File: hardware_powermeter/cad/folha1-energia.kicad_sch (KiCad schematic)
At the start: 24 parts, among them J101 conector magnetico 6 vias, J102 JST SM02B-SRSS-TB, U101 nPM1100-QDAB, U102 MAX17048G+T10

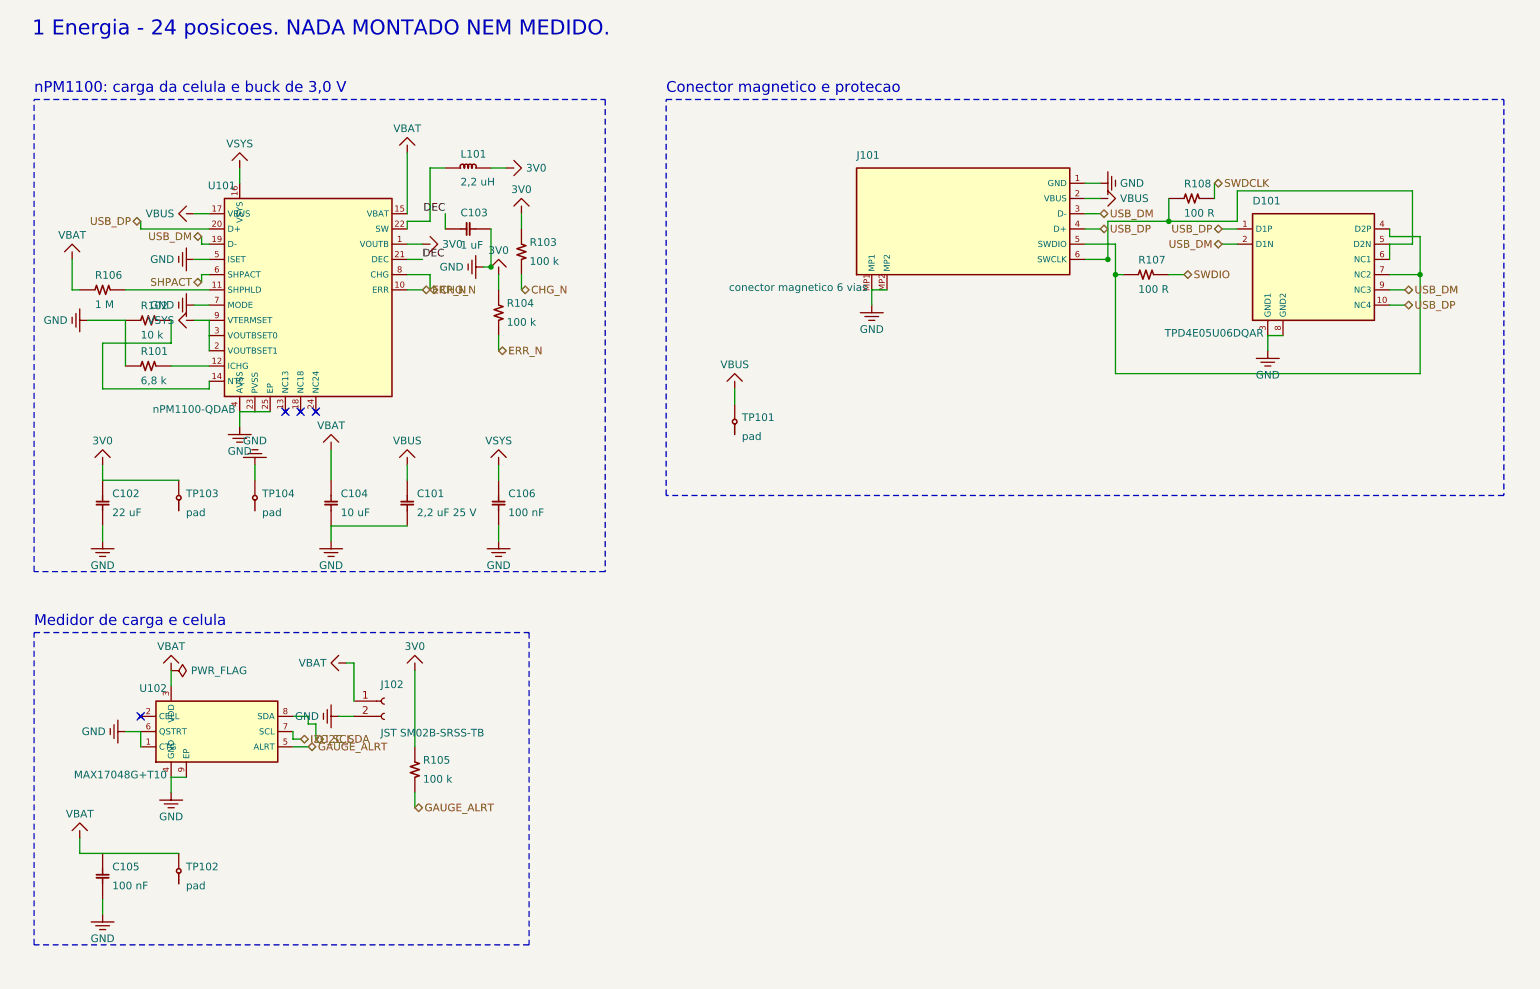
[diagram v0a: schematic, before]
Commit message: feat(hardware): 48 x 16 mm board and a 53,4 x 19,4 x 8,5 mm pod
The board came down from 60 to 48 mm and the pod from 65,4 x 19,4 x 10,5
to 53,4 x 19,4 x 8,5, with the mass estimate at 11,4 g against the 20 g
of the class. The height now meets the target exactly, because the cell
shrank from 4,0 to 2,5 mm: the owner's 5 kOhm decision takes the meter
from 3,9 to 1,5 mA while pedalling, so 50 hours ask for about 75 mAh and
a 100 mAh pouch is enough. The six-way connector stays, in two rows of
three instead of a single row, which gave back about 7 mm of length
without losing a way, and the Tag-Connect went: with SWD on the cable it
was duplicated copper.

It is NOT manufacturable yet, and the numbers say why rather than a
hopeful adjective: the design rule check finds 0 errors but 16
connections still open. One of them, ERR_N, has no copper at all while
the router reported "98 routed, 0 nets left out", so the router's own
accounting is wrong, not just its routing. Disabling the pruning of
dangling tracks was tried first and changed nothing, which clears the
pruning. A second routing pass made it worse, 21 open and three pairs of
vias too close: the pass is not incremental, it re-routes from scratch
into a different result.

Two more real defects are recorded: the placer cannot seat C403 and
C308, carrying them 11 to 13 mm from the part they decouple, and three
pod rules fail, the back-face bodies against the cell, the rib at zero
and a back pad under a pillar.

The layer drawings print properly for the first time. kicad-cli 8.0.6
does not have --page-size-mode or --exclude-drawing-sheet, which are
KiCad 9 options, so the export was failing outright and, before that,
putting a 1:1 board in the corner of an empty sheet. The flags are now
tried and dropped if unknown, and the board is cropped with fitz
instead: 5:1, centred, scale bar and title block.
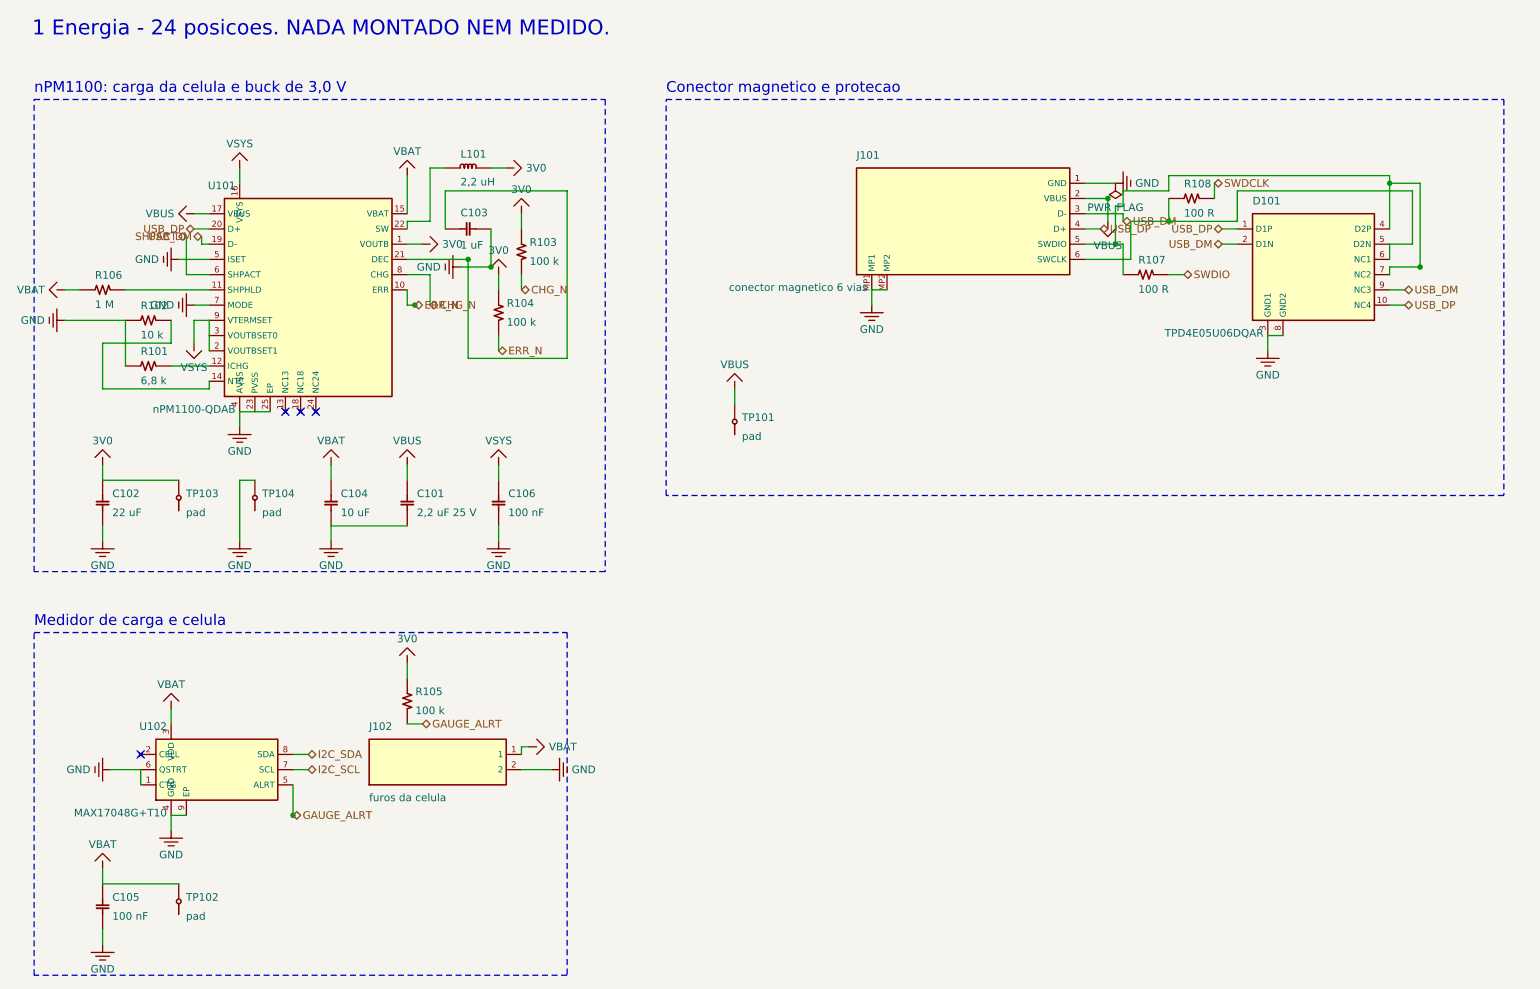
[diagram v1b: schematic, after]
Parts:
- J101: footprint pmeter:Pogo_Magnetico_6P_P2.5mm -> pmeter:Pogo_Magnetico_6P_2x3_P2.5mm
- J102: value JST SM02B-SRSS-TB -> furos da celula; footprint Connector_JST:JST_SH_SM02B-SRSS-TB_1x02-1MP_P1.00mm_Horizontal -> pmeter:Furos_Celula_2x1.5mm_P2.5mm
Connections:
- net DEC: no longer names the net of C103.1, U101.21 (DEC)
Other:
- moved on the sheet: C105, J102, R105, TP102, U102

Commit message: feat(hardware): draw the module for real, and bond the pod to flat metal
Two things the owner asked for, and one the second of them found.

The module gets a body instead of a box. Every DIMENSION is off the maker's
mechanical drawing - the one the footprint is generated from, which closes on
itself three independent ways - and every COLOUR is read off the product
photo, and that difference is recorded rather than smoothed over: a dimension
that closes three ways is evidence, a colour from a photograph is a reading.
It is not one box, because the part is not one box and drawing it as one
hides what decides the layout: a BLACK printed circuit (Holyiot's photo, not
the green of the ME54BS13), a shield can that reads dark rather than as
bright tin, the CERAMIC ANTENNA as an ivory block with metallised ends
sitting outside the can in the 3,80 mm band the drawing keeps clear of pads,
and the gold pads on the underside. Forty-one solids.

It is drawn 2,40 mm tall, and that is a RESERVATION, not a measurement: the
advert gives no height at all. A can over a 0,80 mm board runs 1,8 to 2,2 in
this class, so 2,40 has margin, and drawing it at the reservation makes the
body, the lid's ceiling and the new rule PD18 carry the same number - a part
that arrives taller is then caught by a rule instead of by a lid that will
not close.

The owner asked for the open questions to be measured rather than waited for,
so each one became a requirement with a rule that checks it. The crank's
numbers are the CLASS's - Shimano 105 and Ultegra, the narrow end of the
arm's taper, the tight end of road frame clearance - and PD17 measures the
pod against them. It failed on the first run, and the finding is real: the
arm's inner face is not flat across. A fillet of about 2,5 mm on each side
leaves only 15 of the class's 20 mm flat, and a 19,0 mm pod bonded across its
whole underside would sit on those radii on both sides - adhesive thick at
the edges, thin in the middle, and a joint that peels from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
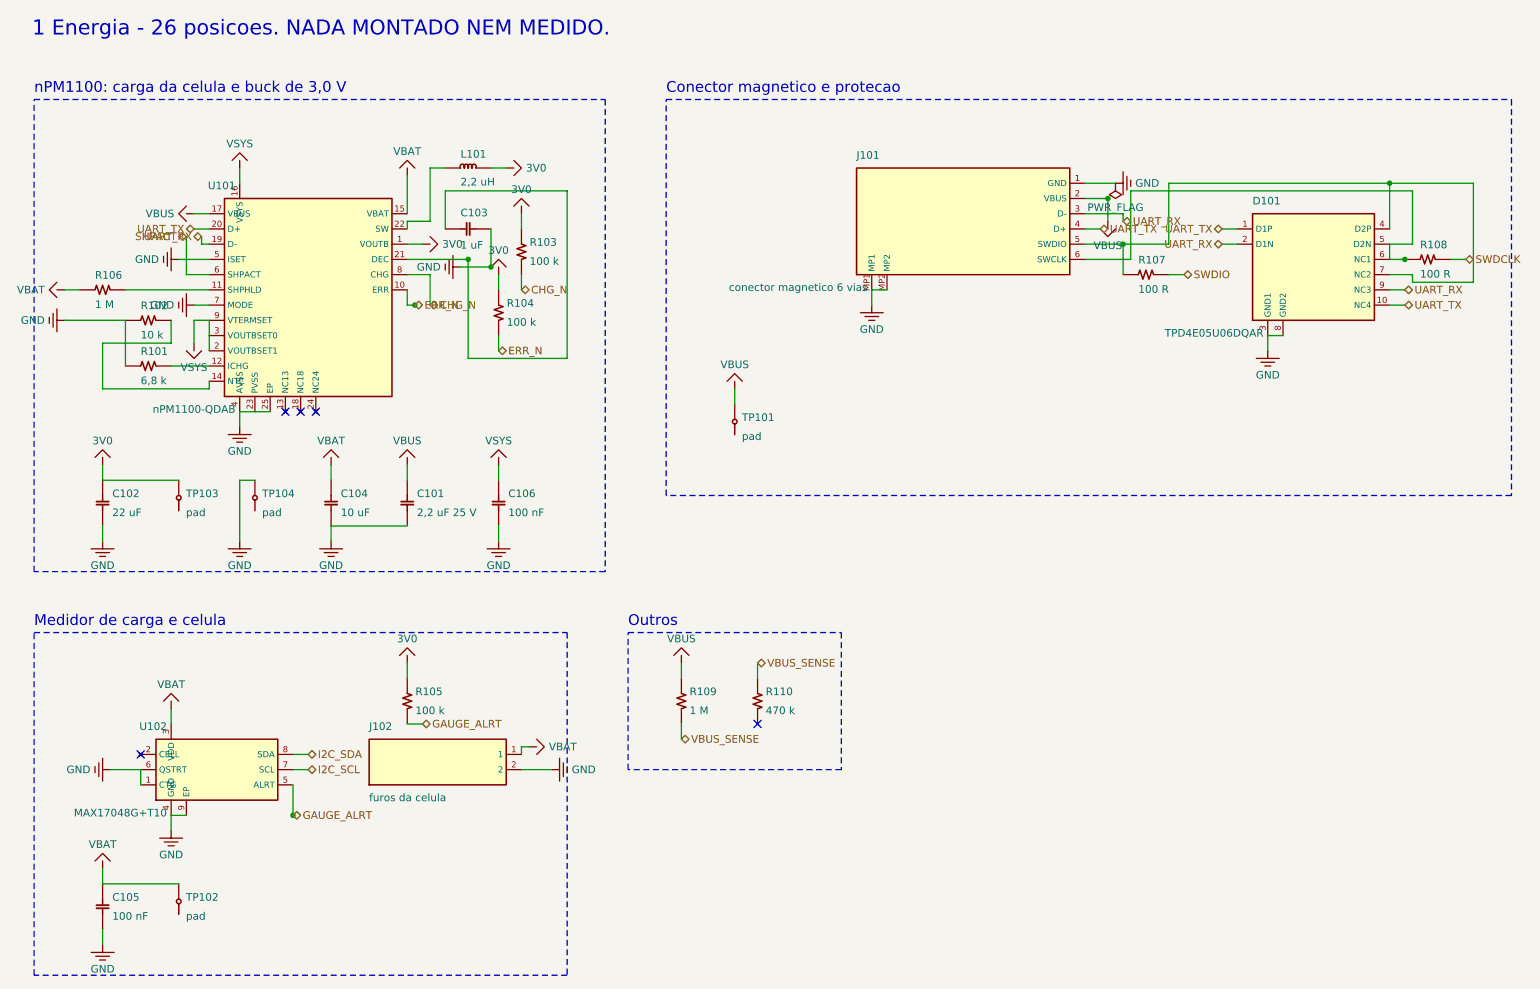
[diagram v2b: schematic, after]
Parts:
- added R109: 1 M, Resistor_SMD:R_0402_1005Metric, symbol pmeter:R109
- added R110: 470 k, Resistor_SMD:R_0402_1005Metric, symbol pmeter:R110
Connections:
- net VBUS: now also R109.1
- net USB_DM renamed UART_RX
- net USB_DP renamed UART_TX
- new net VBUS_SENSE: R109.2, R110.1
- no-connect marks 4 -> 5
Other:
- note added: "1 Energia - 26 posicoes. NADA MONTADO NEM MEDIDO."
- note added: "Outros"
- note removed: "1 Energia - 24 posicoes. NADA MONTADO NEM MEDIDO."
- moved on the sheet: R108

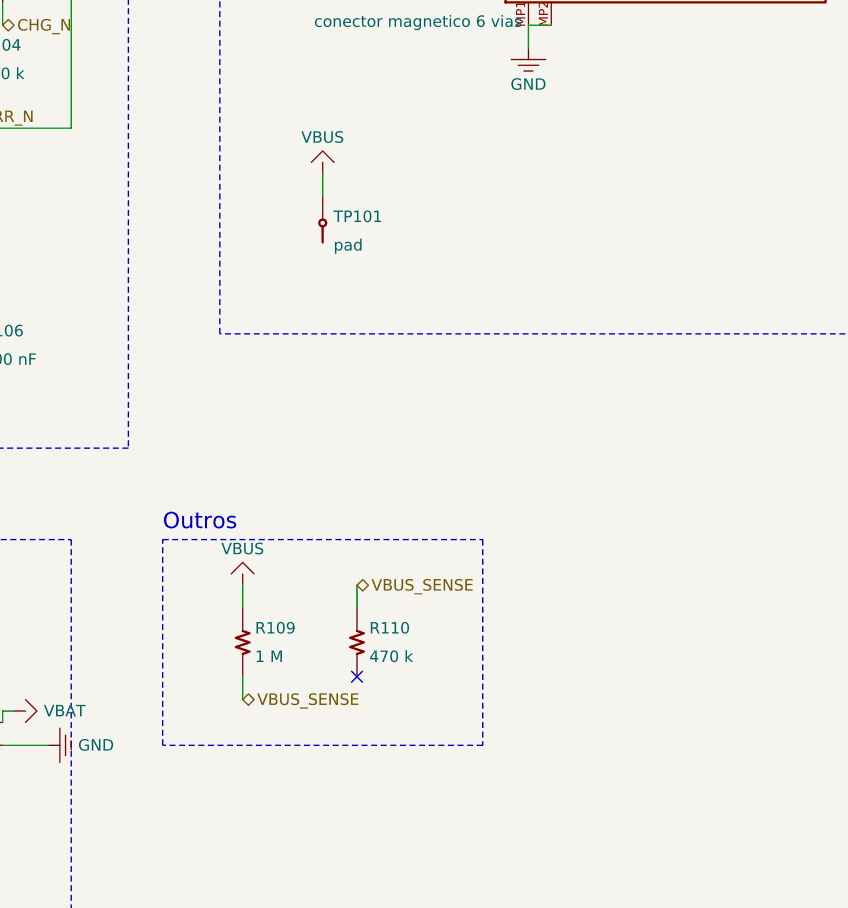
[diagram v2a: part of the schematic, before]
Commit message: docs(docs): bring every page to the module, the cell and the numbers of today
The whole documentation still described the ME54BS13 and a pod built
around a cell that does not exist. What changed, page by page:

- the module: HOLYIOT-26001-A (nRF54L15, ceramic antenna, 36 pads,
  10,0 x 12,5) everywhere the old one was named, with the land pattern
  section rewritten around what can and cannot be verified;
- the board: 47 x 14 mm, one M1,6 hole, no cut-out under the antenna --
  a ceramic antenna wants a clear region touching an edge, not an
  opening;
- the pod: 55,7 x 19,0 x 10,0 mm and 13,3 g, and the cell that raised it.
  The old page said "100 mAh, 2,5 mm thick"; in 23 x 11 x 2,5 a pouch
  cell holds about 49 mAh, which at 1,5 mA is 32 h against a 50 h
  requirement. The cell that fits and answers is a 401123 class part,
  >= 78 mAh, and at 0,68 mA it gives 114 h;
- the bridge resistance, which docs/06 still called an open decision: it
  was taken, and the part is the S5229 of 5 kohm;
- the memory figures, re-measured from a clean build of all three
  targets, and the free-pin statement, now separating the nine GPIO that
  exist on this board from the three that exist only on the SoC;
- the stack of the pod's `serial` thread, measured with CONFIG_STACK_USAGE
  on pmboard/nrf54l15/cpuapp: 856 B of project frames, 1,5 KB of slack.

The README gains the full set of views -- product, pod and board -- and
a row for the battery.
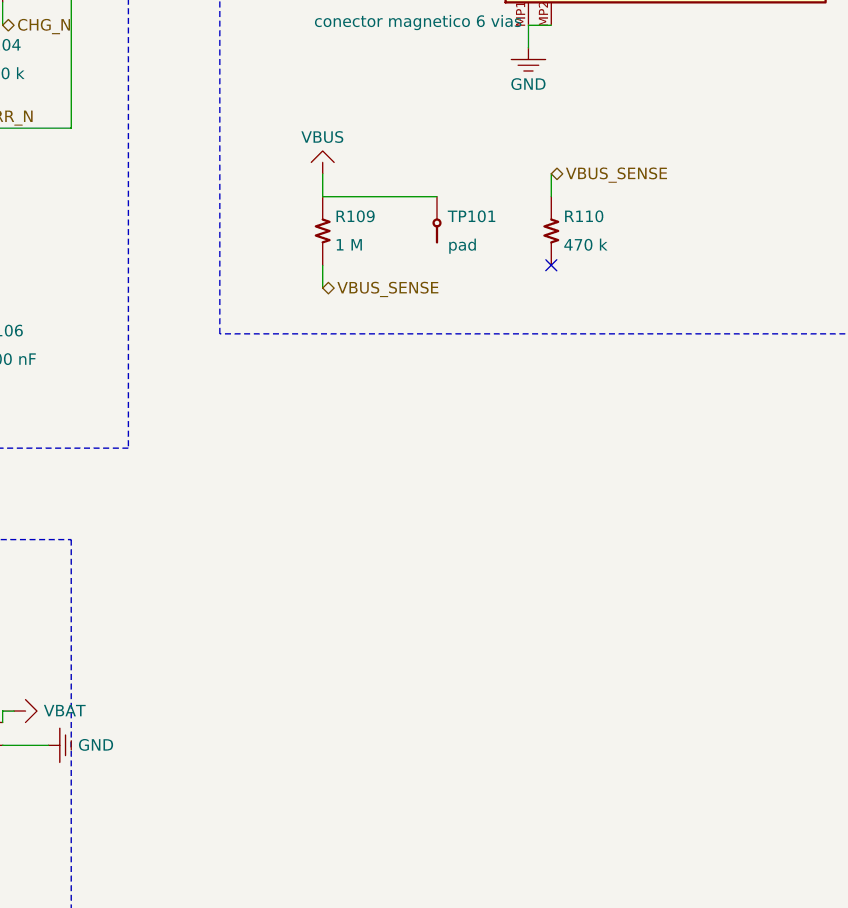
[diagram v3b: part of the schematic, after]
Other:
- note removed: "Outros"
- moved on the sheet: R109, R110, TP101

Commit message: feat(hardware): the cell enters by connector, and the board generates again
The owner asked for the cell to arrive with its two wires AND its plug, and
for the board's receptacle to be the angled one - mouth parallel to the board,
not the vertical kind. Both are done, and the way there uncovered two defects
that had nothing to do with connectors.

THE CONNECTOR. J102 was two plated holes for hand-soldered wire since
2026-09-26, and the argument for that was good: it took the tallest part off
the board, 2.90 mm, which set the lid's ceiling by itself. What it did not see
is that the cell you BUY arrives with a plug, so holes mean cutting it off and
soldering bare 30 AWG inside a 20 mm box, with the cell no longer replaceable.

The series was measured, not guessed. All three were placed on the board and
the pod measured with each, from the KiCad library's 3D models:

  PH 2,0  S2B-PH-SM4-TB   4,85 mm   5,9 x 7,6   pod 9,70   17,7 g  24 of 32
  GH 1,25 SM02B-GHS-TB    4,24 mm   5,8 x 5,0   pod 9,04      -        -
  SH 1,0  SM02B-SRSS-TB   2,90 mm   4,3 x 4,0   pod 7,70   14,5 g  30 of 32

PH is what pouch cells ship with - confirmed on three documented parts - and
it was tried first. Its bill does not close: it would force the magnetic
connector up to 5,35 mm (the reserved place is 3,2, and with the ceiling at
5,15 its face would sit 2,0 mm BELOW the lid - the charging port would stop
existing), widen the channel by 1,8 mm for the plug, leave the screw heads
1,1 mm over the height target, take the blind screw hole to 5,5:1, and put the
glue-plus-pod stack at 10,2 mm against the 10,0 of frame clearance the project
reserved. SH costs one line on the cell's order instead: pouch makers sell the
connector as an option.

THE CABLE CUT the owner asked not to forget was already there - 3,4 mm through
the ribs and the floor - but it had been cut for two bare wires. With a plug,
PD21 and PD32 caught that the left screw's boss stood right in front of it,
and that the plug had 0,0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
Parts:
- J102: footprint pmeter:Furos_Celula_2x1.5mm_P2.5mm -> Connector_JST:JST_SH_SM02B-SRSS-TB_1x02-1MP_P1.00mm_Horizontal
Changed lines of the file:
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@@
 			(effects (font (size 1.27 1.27)) (justify left top))
 		)
-		(property "Footprint" "pmeter:Furos_Celula_2x1.5mm_P2.5mm"
+		(property "Footprint" "Connector_JST:JST_SH_SM02B-SRSS-TB_1x02-1MP_P1.00mm_Horizontal"
 			(at 87.63 144.78 0)
 			(effects (font (size 1.27 1.27)) (hide yes))
